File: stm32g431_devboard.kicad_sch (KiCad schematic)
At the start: 0 parts

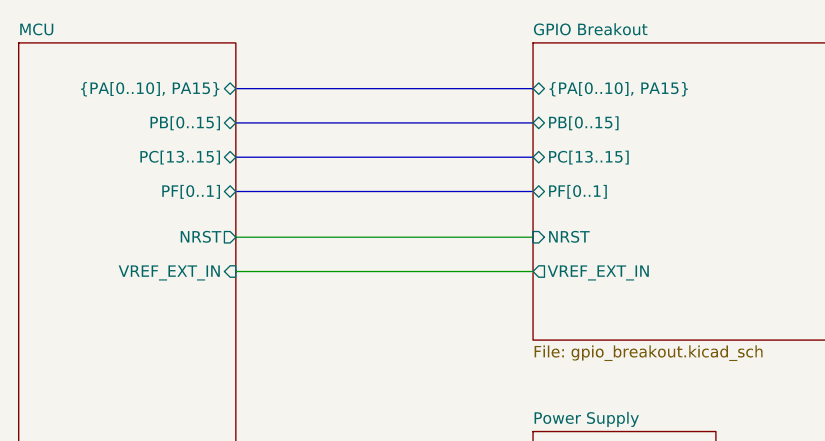
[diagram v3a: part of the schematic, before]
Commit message: v0.2: low-power redesign — single LDO, ideal diodes, LSE, castellated SWD
Power supply:
- Replace dual LDO (AP2112K + MCP1700) with single TPS7A0233PDBV
  (25 nA Iq nanopower; EN tied to IN per datasheet)
- Replace SS14 Schottky diodes with LM66100 ideal diode controllers
  in diode-OR configuration (CE tied to VOUT for RCB mode)
- Remove jumpers J2 (LDO_SEL), J3 (LED_VBUS), J4 (LED_3V3)
- Replace JST battery connector with castellated header J_VBAT
- Replace J5 IMEAS jumper with 0R bridge
- Rename diode-OR output net to VDC

MCU:
- Add LSE crystal Y1 (32.768 kHz ABS07) with 18 pF load caps
- Dedicate PC14/PC15 to LSE oscillator (removed from J_R breakout)
- Wire BOOT0 net to PB8 (requires nBOOT_SEL=0 option byte)
- Replace VREF_SEL 3-pin jumper with two 0R bridges
- Change reset/boot buttons to C&K PTS810SJM250SMTR (smaller)
- Remove user button SW3

SWD:
- J6 changed from 1x05 THT to 1x06 castellated header
- Pinout follows ST-Link V2 Mini: 3V3/SWCLK/GND/SWDIO/NRST/SWO
- SWO (PB3) shared with GPIO breakout

GPIO breakout:
- Move PA2/PA3 from J_L to J_R (filling former PC14/PC15 slots)
- Add +3V3 and extra GND to J_L in vacated positions
- Break out PC13 to J_R
- J9 UART connector: SMD hand-solderable, no series resistors

Re-annotate all references for sequential numbering.
ERC: clean (with documented exclusion for diode-OR power outputs).
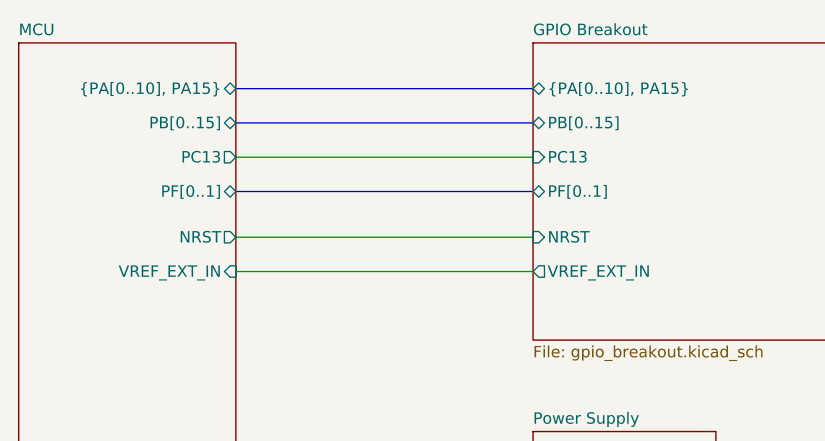
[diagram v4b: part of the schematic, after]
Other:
- sheet GPIO Breakout ports: added PC13; removed PC[13..15]
- sheet MCU ports: added PC13; removed PC[13..15]
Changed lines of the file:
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@@
 	(title_block
 		(title "${PROJECT_NAME}, Guillermo Gil")
-		(rev "v.0.1")
+		(rev "v.0.2")
 	)
 	(wire
@@
 		)
 	)
+	(wire
+		(pts
+			(xy 88.9 77.47) (xy 121.92 77.47)
+		)
+		(stroke
+			(width 0)
+			(type default)
+		)
+	)
 	(bus
 		(pts
 			(xy 88.9 69.85) (xy 121.92 69.85)
-		)
-		(stroke
-			(width 0)
-			(type default)
-		)
-	)
-	(bus
-		(pts
-			(xy 88.9 77.47) (xy 121.92 77.47)
 		)
 		(stroke
@@
 			)
 		)
-		(pin "PC[13..15]" bidirectional
-			(at 121.92 77.47 180)
-			(effects
-				(font
-					(size 1.27 1.27)
-				)
-				(justify left)
-			)
-		)
 		(pin "PF[0..1]" bidirectional
 			(at 121.92 81.28 180)
@@
 		(pin "VREF_EXT_IN" output
 			(at 121.92 90.17 180)
+			(effects
+				(font
+					(size 1.27 1.27)
+				)
+				(justify left)
+			)
+		)
+		(pin "PC13" input
+			(at 121.92 77.47 180)
 			(effects
 				(font
@@
 			)
 		)
-		(pin "PC[13..15]" bidirectional
-			(at 88.9 77.47 0)
-			(effects
-				(font
-					(size 1.27 1.27)
-				)
-				(justify right)
-			)
-		)
 		(pin "USB_DP" bidirectional
 			(at 88.9 113.03 0)
@@
 			(effects
 				(font
+					(size 1.27 1.27)
+				)
+				(justify right)
+			)
+		)
+		(pin "PC13" output
+			(at 88.9 77.47 0)
+			(effects
+				(font

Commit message: Finish routing
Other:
- sheet MCU ports: added USB_N, USB_P; removed USB_DM, USB_DP
- sheet Power Supply ports: added USB_N, USB_P; removed USB_DM, USB_DP
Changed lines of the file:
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@@
 			)
 		)
-		(pin "USB_DM" bidirectional
+		(pin "USB_N" bidirectional
 			(at 121.92 110.49 180)
 			(effects
@@
 			)
 		)
-		(pin "USB_DP" bidirectional
+		(pin "USB_P" bidirectional
 			(at 121.92 113.03 180)
 			(effects
@@
 			)
 		)
-		(pin "USB_DP" bidirectional
+		(pin "USB_P" bidirectional
 			(at 88.9 113.03 0)
 			(effects
@@
 			)
 		)
-		(pin "USB_DM" bidirectional
+		(pin "USB_N" bidirectional
 			(at 88.9 110.49 0)
 			(effects
